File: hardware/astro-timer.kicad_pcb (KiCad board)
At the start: 2 copper layers, 66.3 x 48.8 mm, 27 parts, among them J1 Conn_01x02_Male, J2 AVR-ISP-6, J3 AudioJack2, SW1 SW_SPST, SW2 SW_Push, SW3 SW_Push, SW4 Rotary_Encoder_Switch, U1 ATmega328P-PU, U2 LTV-817M, Y1 Crystal

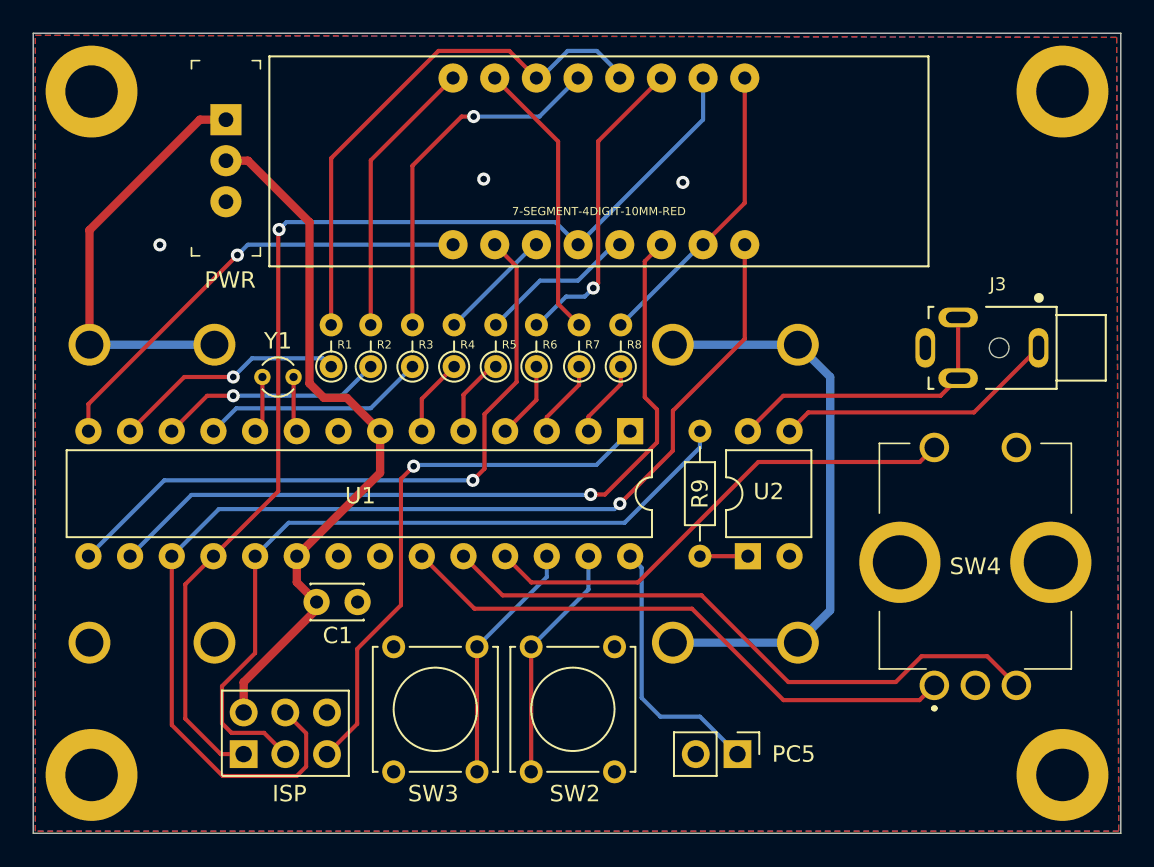
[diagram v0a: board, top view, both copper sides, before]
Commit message: add crystal caps
and do a bit of odd routing to put a ground plane under
the crystal, while we're at it

the prior version of this device worked fine without either
of these things, but the datasheet asks for both, and since
I'm revising the board anyway
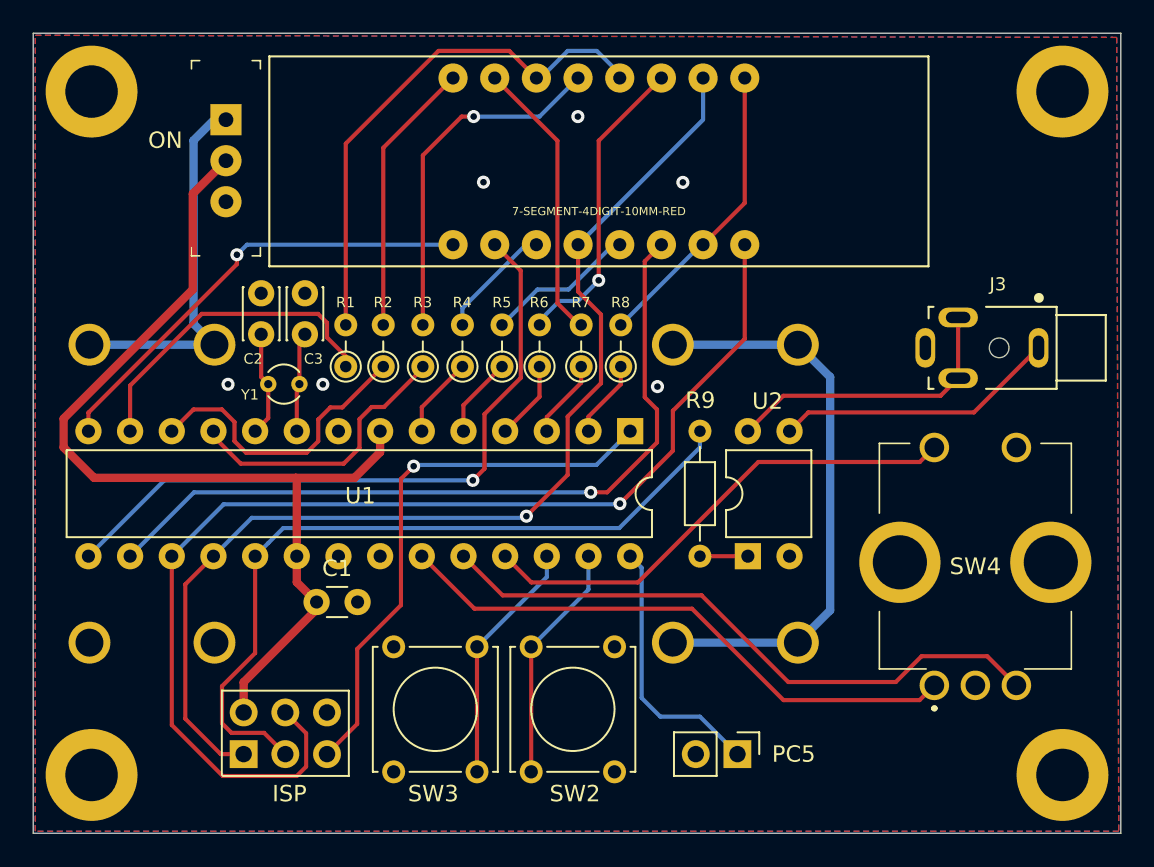
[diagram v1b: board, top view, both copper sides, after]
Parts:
- added C2: C, Capacitor_THT:C_Disc_D3.0mm_W2.0mm_P2.50mm, F.Cu at (96.3, 105.2)
- added C3: C, Capacitor_THT:C_Disc_D3.0mm_W2.0mm_P2.50mm, F.Cu at (99.0, 105.2)
- C1: footprint Capacitor_THT:C_Disc_D3.0mm_W2.0mm_P2.50mm -> Capacitor_THT:C_Disc_D3.0mm_W1.6mm_P2.50mm
- moved R1 0.89 mm to (101.5, 107.1)
- moved R2 0.76 mm to (103.8, 107.1)
- moved R3 0.63 mm to (106.2, 107.1)
- moved Y1 0.56 mm to (96.7, 108.2)
- moved R4 0.51 mm to (108.6, 107.1)
- moved R5 0.38 mm to (111.0, 107.1)
- moved R6 0.19 mm to (113.3, 107.1)
- moved R7 0.13 mm to (115.8, 107.1)
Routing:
- net VCC: track 43.6 -> 60.2 mm
- net /a: track 14.3 -> 20.0 mm, vias 1 -> 0
- net /b: track 13.8 -> 18.2 mm, vias 1 -> 0
- net /c: track 13.8 -> 17.3 mm
- net Net-(C3-Pad1): track 3.38 -> 6.57 mm
- net Net-(C2-Pad1): track 3.49 -> 6.20 mm
- net Net-(BT1-PadPWR@): track 25.7 -> 23.1 mm
- net /dige: track 68.9 -> 67.5 mm
- net GND: vias 3 -> 6
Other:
- board text added: "ON"
- board text removed: "PWR"

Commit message: important
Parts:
- moved SW2 9.21 mm to (112.8, 131.9), turned to 90 degrees
- moved SW3 0.14 mm to (104.3, 131.9)
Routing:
- net /a: track 20.0 -> 14.8 mm
- net /b: track 18.2 -> 14.5 mm
- net /sw1: track 14.6 -> 13.9 mm
- net /c: track 17.3 -> 16.7 mm
- net GND: vias 6 -> 5
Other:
- board text added: "SELECT"
- board text added: "START"

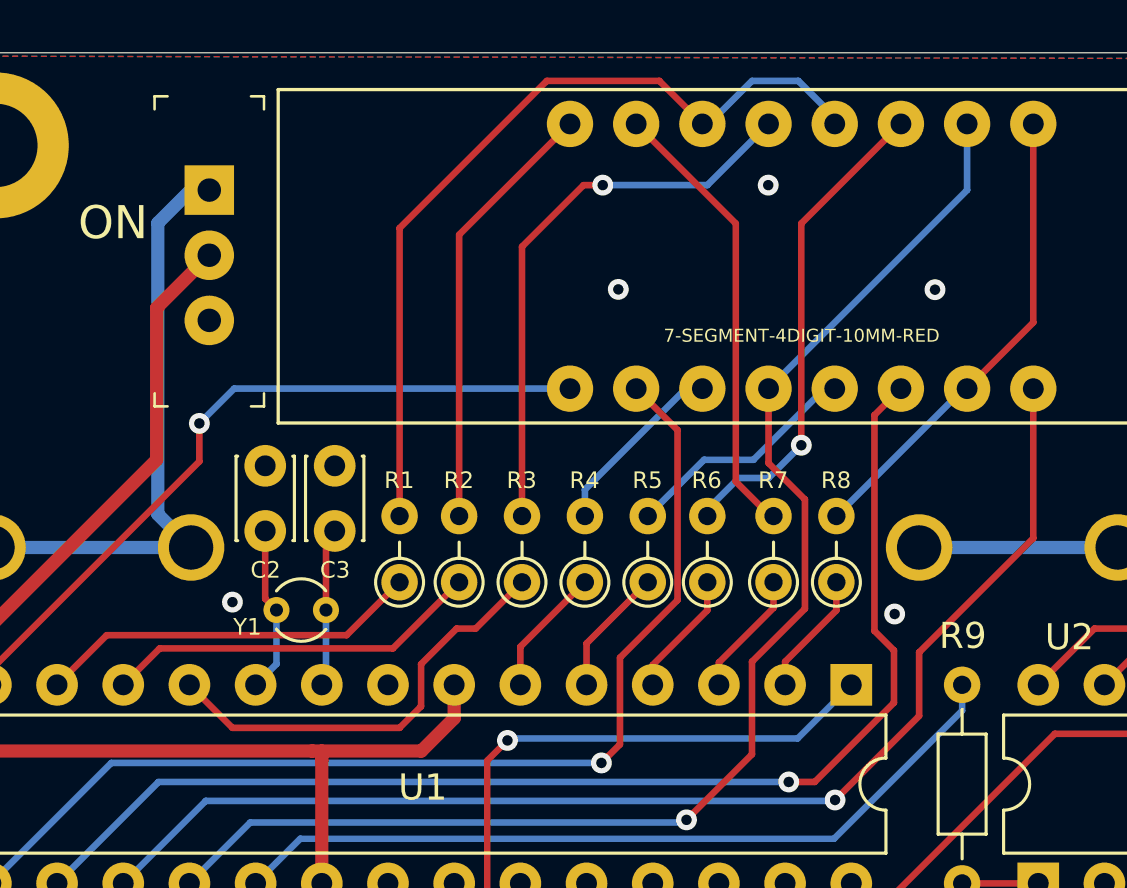
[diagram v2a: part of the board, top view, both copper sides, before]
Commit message: zomg how do I fail to notice the resistors are misaligned before drawing traces
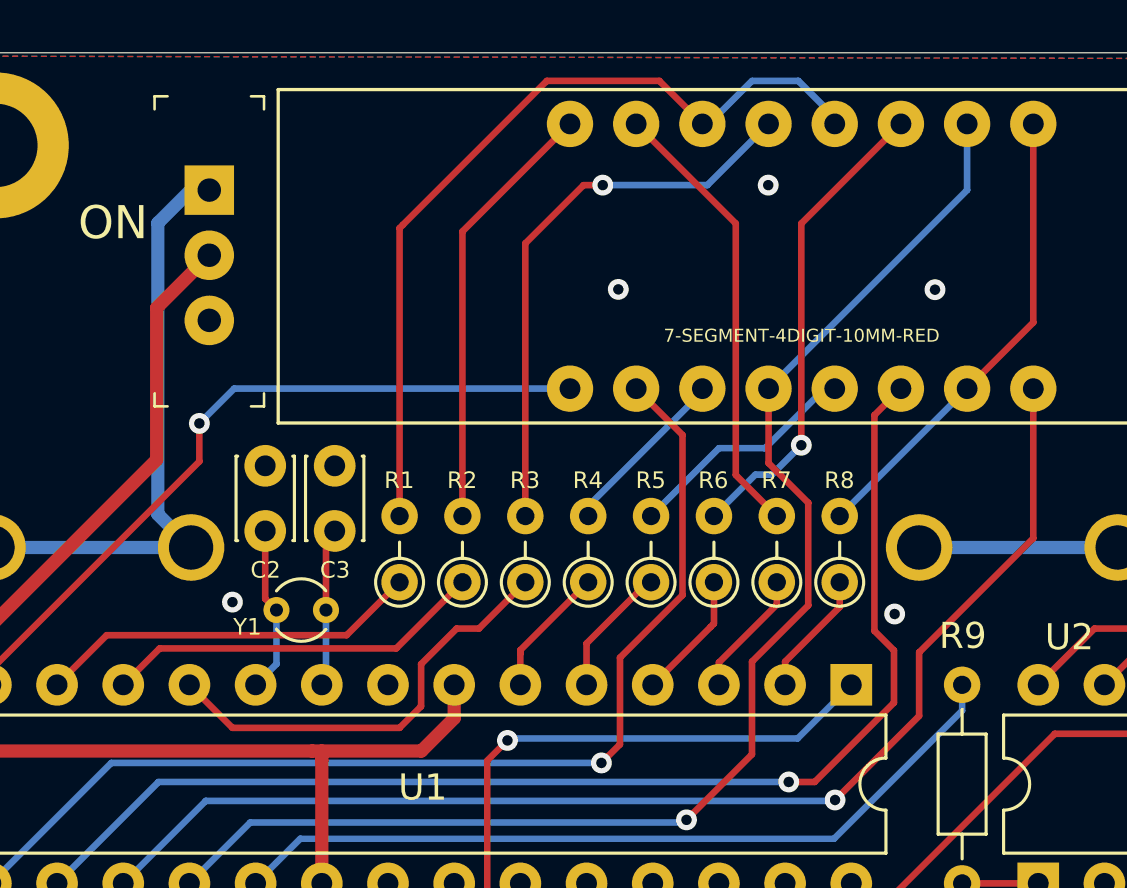
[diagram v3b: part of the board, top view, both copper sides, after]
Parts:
- moved R6 0.25 mm to (113.5, 107.1)
- moved R3 0.13 mm to (106.3, 107.1)
- moved R4 0.13 mm to (108.7, 107.1)
- moved R8 0.13 mm to (118.4, 107.1)
- moved R2 0.13 mm to (103.9, 107.1)
- moved R5 0.13 mm to (111.1, 107.1)
- moved R7 0.13 mm to (116.0, 107.1)
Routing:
- net /f: track 5.12 -> 5.74 mm

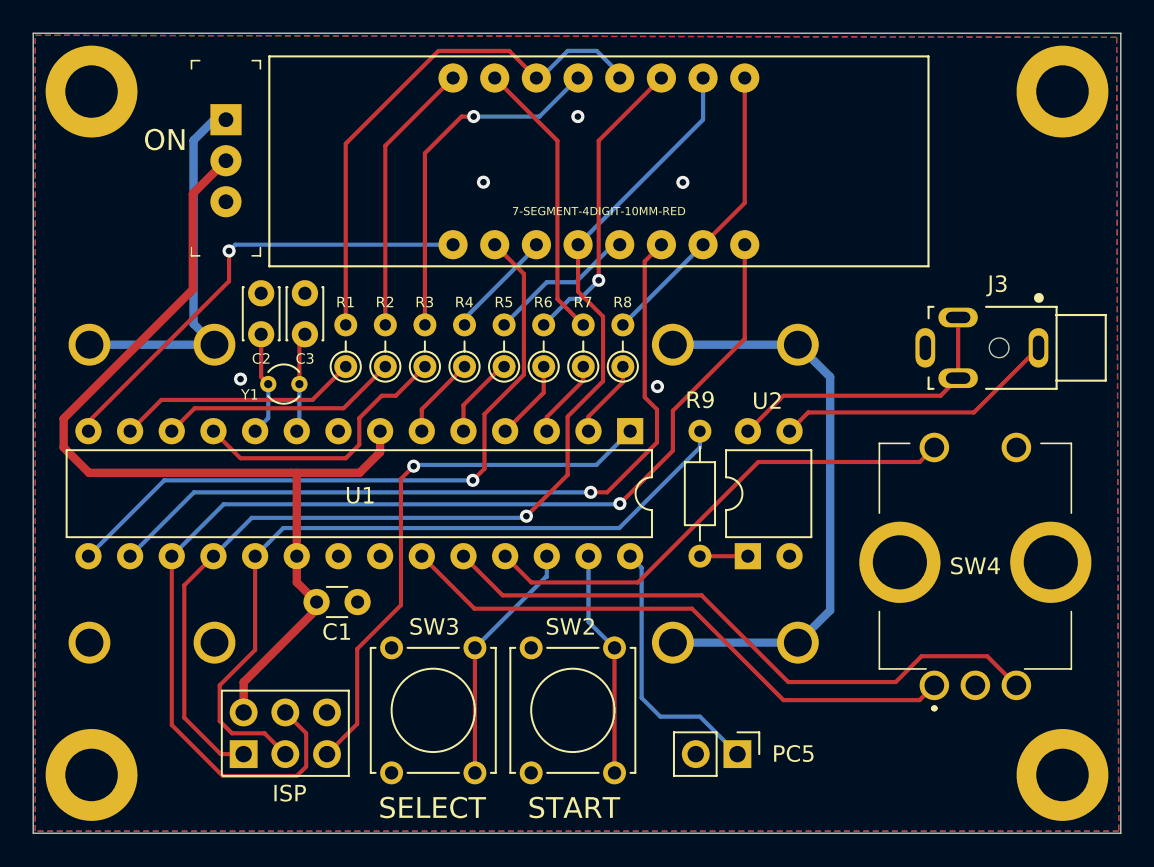
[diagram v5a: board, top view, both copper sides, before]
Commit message: fix battery footprint
sparkfun's library made them 0.02" too wide

maybe that doesn't matter; maybe it was intentional

but I'm going by the book here
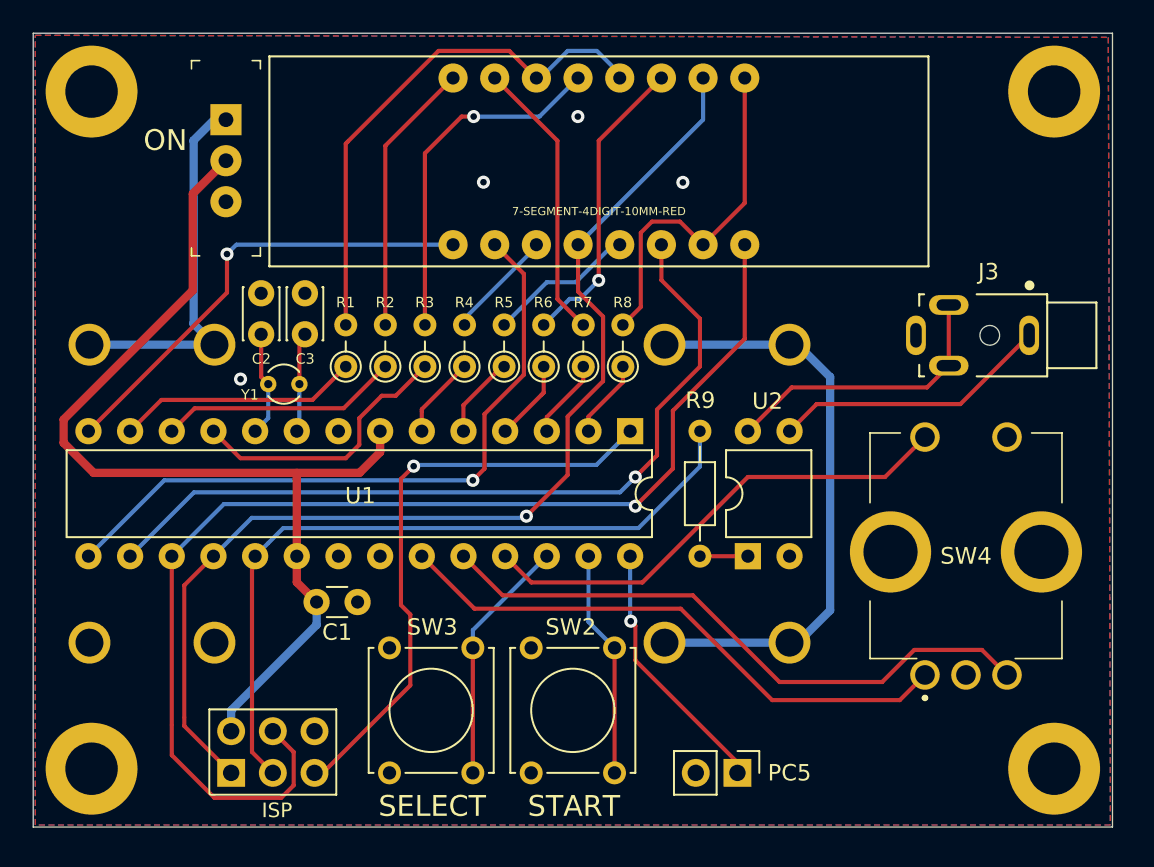
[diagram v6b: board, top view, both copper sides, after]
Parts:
- removed the REF** at (86.0, 132.0)
- removed the REF** at (145.2, 132.0)
- added REF**: MountingHole_3.2mm_M3_DIN965_Pad, MountingHole:MountingHole_3.2mm_M3_DIN965_Pad, F.Cu at (86.0, 131.6)
- added REF**: MountingHole_3.2mm_M3_DIN965_Pad, MountingHole:MountingHole_3.2mm_M3_DIN965_Pad, F.Cu at (144.7, 131.6)
- moved J2 1.37 mm to (94.5, 131.9)
- moved J1 1.14 mm to (125.3, 131.9)
- moved J3 0.95 mm to (143.1, 105.2)
- moved SW4 0.85 mm to (136.8, 125.9)
- moved REF** 0.51 mm to (144.7, 90.4)
- moved BT1 0.25 mm to (107.2, 105.8)
- moved BT2 0.25 mm to (107.2, 124.0)
- moved SW3 0.13 mm to (104.1, 131.9)
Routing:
- net Net-(LED1-Pad7): track 18.3 -> 22.1 mm
- net /rst: track 33.8 -> 36.0 mm
- net /dig3: track 47.8 -> 49.6 mm
- net /dig4: track 71.4 -> 73.1 mm
- net VCC: track 60.3 -> 61.6 mm
- net /pc: track 46.6 -> 45.3 mm
- net /pc5: track 16.2 -> 15.9 mm, vias 0 -> 1
- net GND: vias 5 -> 4
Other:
- board size 66.3 x 48.8 mm -> 65.8 x 48.4 mm

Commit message: battery footprint tweaks
the datasheet also specified a slightly larger hole size
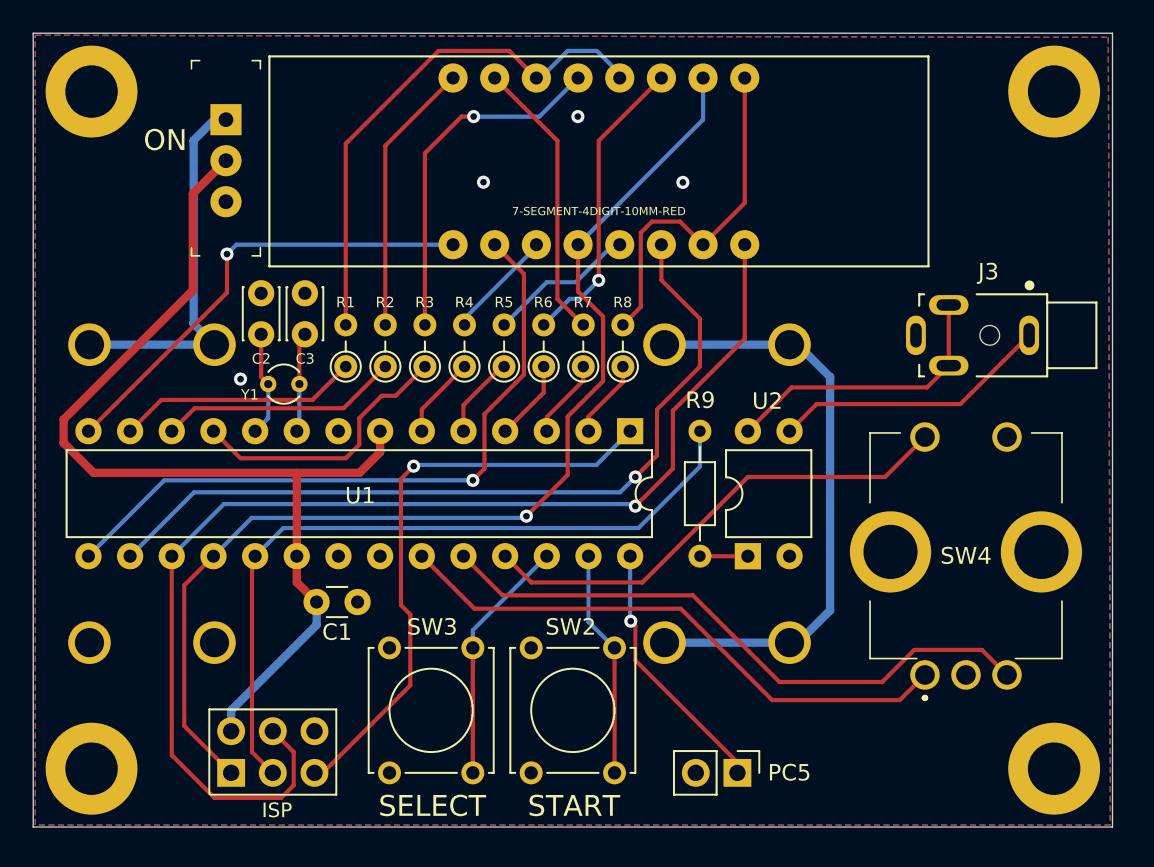
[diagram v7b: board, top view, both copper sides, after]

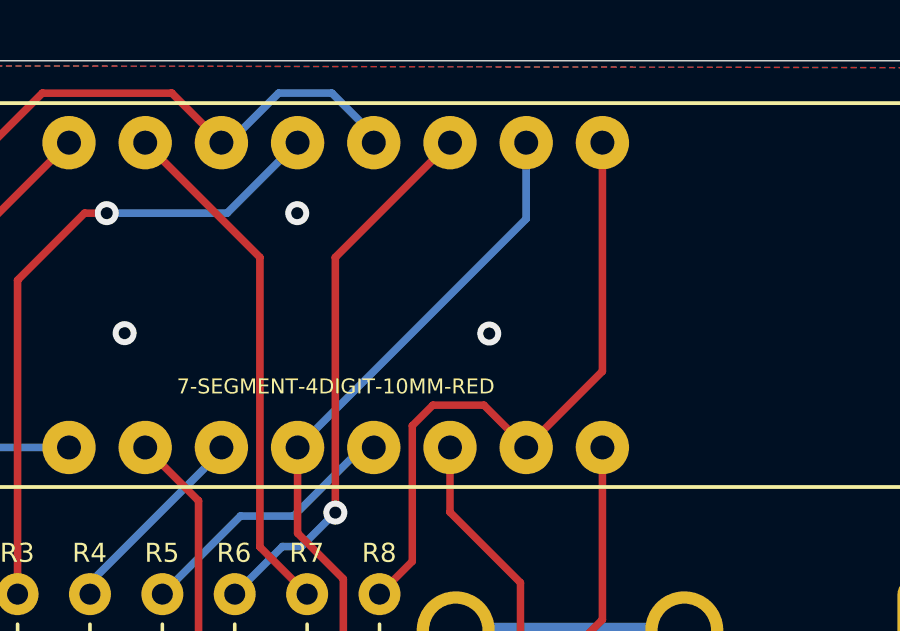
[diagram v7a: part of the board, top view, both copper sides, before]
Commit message: plex apostrophe with C segment
because why not, that's how Lite-On does it

also tweak the ground plane keepouts under the battery clips
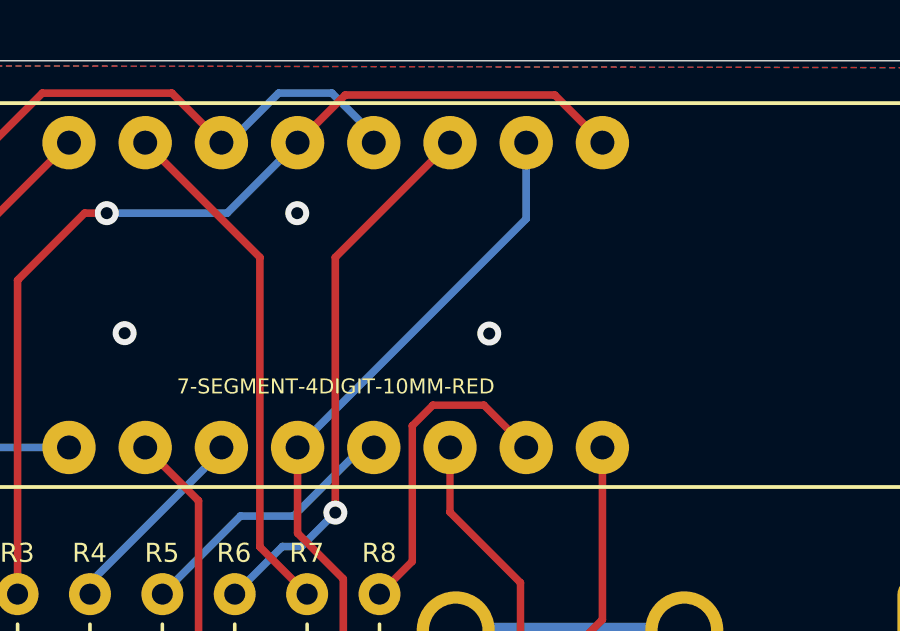
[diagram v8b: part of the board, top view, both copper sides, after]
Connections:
- LED1 pad 9: Net-(LED1-Pad7) -> Net-(LED1-Pad13)
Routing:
- net Net-(LED1-Pad13): track 21.7 -> 33.2 mm
- net Net-(LED1-Pad7): track 22.1 -> 10.9 mm
